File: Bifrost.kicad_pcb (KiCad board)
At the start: 4 copper layers, 68.6 x 53.3 mm, 69 parts, among them J1 OIP, J2 Conn_01x03_Male, J3 Conn_01x03_Male, U2 AD5932, U3 LMH6881, U5 AD5932, X1 SPXO-50M

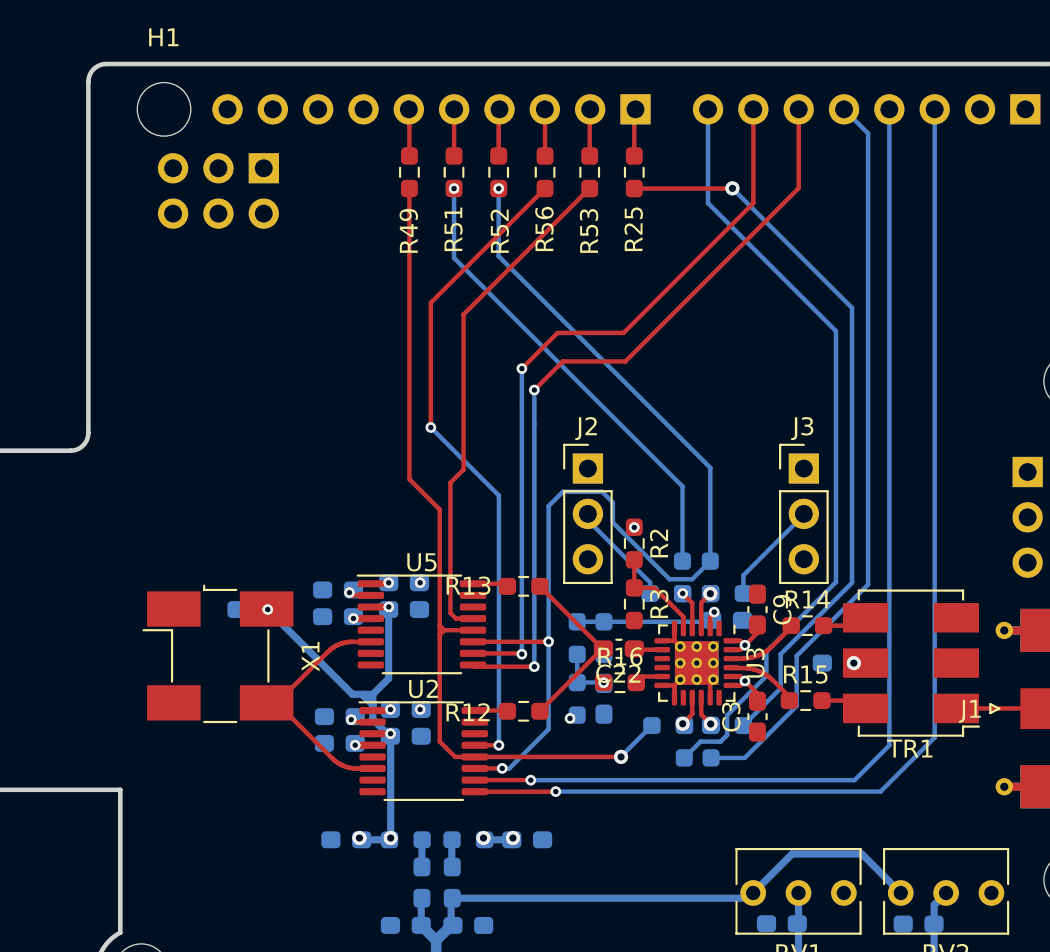
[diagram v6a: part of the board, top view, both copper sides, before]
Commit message: Added SCLF-21.4+ Deleted the superfluous AD5932 Changed the switches for the LMH881 gain from D0&D1 to D2&D3 Re-routed
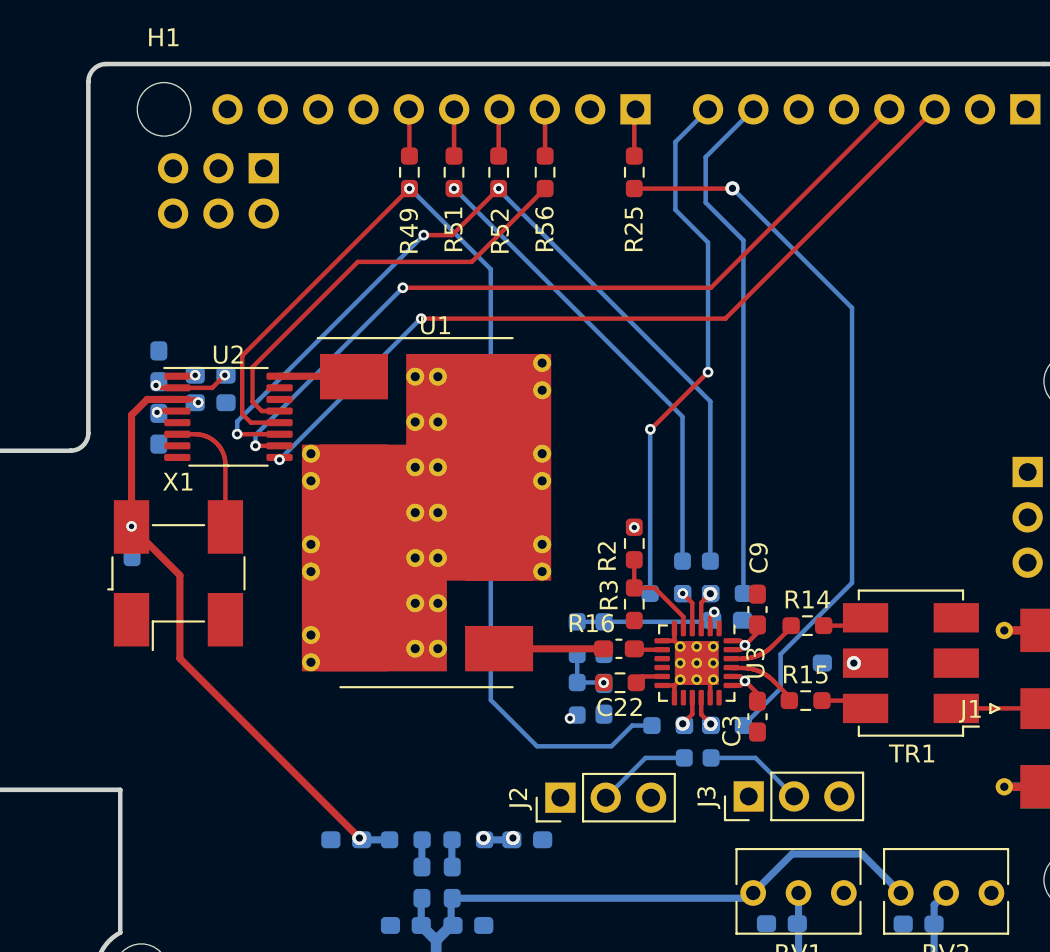
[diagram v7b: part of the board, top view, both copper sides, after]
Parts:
- removed C12: 10n, Capacitor_SMD:C_0603_1608Metric_Pad1.08x0.95mm_HandSolder
- removed C15, C16, C17: 100n, Capacitor_SMD:C_0603_1608Metric_Pad1.08x0.95mm_HandSolder
- removed R12, R13: 50, Resistor_SMD:R_0603_1608Metric_Pad0.98x0.95mm_HandSolder
- removed R53: 300, Resistor_SMD:R_0603_1608Metric_Pad0.98x0.95mm_HandSolder
- removed U5: AD5932, Package_SO:TSSOP-16_4.4x5mm_P0.65mm
- added U1: SCLF-21.4, RF_Mini-Circuits:Mini-Circuits_YY161_LandPatternPL-049, F.Cu at (144.2, 103.5)
- moved C6 22.1 mm to (129.2, 95.3), turned to 90 degrees
- moved C2 21.7 mm to (132.1, 95.8)
- moved U2 21.7 mm to (133.1, 98.1)
- moved C7 21.7 mm to (132.1, 97.3)
- moved C10 20.3 mm to (129.2, 98.8), turned to 270 degrees
- moved J3 18.6 mm to (162.2, 119.4), turned to 90 degrees
- moved J2 18.5 mm to (151.7, 119.4), turned to 90 degrees
- moved C1 7.75 mm to (127.7, 105.1), turned to 90 degrees
- moved X1 5.19 mm to (130.3, 106.9), turned to 0 degrees
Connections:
- AD1 pad 2: /AD1 -> (no net)
- AD1 pad 3: /AD2 -> (no net)
- AD1 pad 5: /AD4 -> (no net)
- AD1 pad 6: /AD5 -> (no net)
- ICSP1 pad 1: /MISO2 -> (no net)
- ICSP1 pad 2: /+5V_Adr_3 -> (no net)
- ICSP1 pad 3: /SCK2 -> (no net)
- ICSP1 pad 4: /MOSI2 -> (no net)
- ICSP1 pad 5: /RESET2 -> (no net)
- ICSP2 pad 1: /MISO_0 -> (no net)
- ICSP2 pad 2: /+5V_Ard_0 -> (no net)
- ICSP2 pad 3: /SCK_0 -> (no net)
- ICSP2 pad 4: /MOSI_0 -> (no net)
- ICSP2 pad 5: /RESET_0 -> (no net)
- IOH1 pad 10: /SCL -> (no net)
- IOH1 pad 2: /IO9 -> (no net)
- IOH1 pad 8: /AREF -> (no net)
- IOH1 pad 9: /SDA -> (no net)
- IOL1 pad 1: /IO0 -> (no net)
- IOL1 pad 2: /IO1 -> (no net)
- IOL1 pad 5: /IO4 -> (no net)
- IOL1 pad 6: /IO5 -> (no net)
- POWER1 pad 1: Net-(POWER1-Pad1) -> (no net)
- POWER1 pad 3: /RESET -> (no net)
- POWER1 pad 4: /+3V3 -> (no net)
- POWER1 pad 5: /+5V_Ard_1 -> (no net)
- POWER1 pad 8: /VIN -> (no net)
- R18 pad 2: Net-(J2-Pad2) -> /IO7
- R20 pad 2: Net-(J3-Pad2) -> /IO6
- R22 pad 2: /IO7 -> Net-(J2-Pad2)
- R24 pad 2: /IO4 -> Net-(J3-Pad2)
- TR1 pad 2: Net-(TR1-Pad2) -> (no net)
- U2 pad 7: Net-(U2-Pad7) -> (no net)
- U2 pad 8: Net-(U2-Pad8) -> (no net)
- U3 pad 1: Net-(U3-Pad1) -> (no net)
- U3 pad 10: Net-(U3-Pad10) -> (no net)
- U3 pad 14: Net-(U3-Pad14) -> (no net)
- U3 pad 18: Net-(U3-Pad18) -> (no net)
- U3 pad 9: Net-(U3-Pad9) -> (no net)
- X1 pad 1: Net-(X1-Pad1) -> (no net)
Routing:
- net /IO5: track 42.9 -> 0.00 mm, vias 2 -> 0
- net /IO4: track 41.6 -> 0.00 mm
- net /SEN2: track 28.4 -> 0.00 mm
- net /IO2: track 62.2 -> 44.8 mm, vias 1 -> 2
- net /IO3: track 59.7 -> 45.0 mm, vias 1 -> 2
- net /IO7: track 43.5 -> 30.0 mm, vias 0 -> 2
- net /SCK: track 47.0 -> 60.0 mm
- net /SEN: track 36.8 -> 24.2 mm, vias 2 -> 0
- net /IO6: track 40.8 -> 29.1 mm, vias 2 -> 0
- net /SDI: track 60.1 -> 48.9 mm
- net VDD: track 26.0 -> 34.9 mm, vias 5 -> 3
- net /Sheet61C59086/MCLK: track 13.4 -> 7.16 mm
- net Net-(C22-Pad2): track 9.95 -> 5.88 mm
- net /IO9: track 2.63 -> 0.00 mm
- net /Sheet61C59086/Fout: track 1.79 -> 4.18 mm
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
